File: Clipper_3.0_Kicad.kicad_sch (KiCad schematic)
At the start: 25 parts, among them J1 Conn_01x08_Pin, J10 Conn_01x19_Socket, J11 Screw_Terminal_01x02, J12 Conn_01x01_Socket, J13 Conn_01x01_Socket, J14 Conn_01x01_Socket, J15 Conn_01x01_Socket, J16 Conn_01x01_Pin, J17 Conn_01x01_Pin, J18 Conn_01x01_Pin, J19 Conn_01x01_Pin, J2 Conn_01x08_Pin, J3 Conn_01x08_Pin, J4 Conn_01x08_Socket, J5 Conn_01x08_Socket, J6 Conn_01x08_Socket, J7 Conn_01x19_Pin, J8 Conn_01x19_Pin, J9 Conn_01x19_Socket, M1 Motor_Derecho, M2 Motor_Îzquierdo, U1 ESP32-DevKitC, U2 TB6612FNG_MODULE, U3 GY-521 MODULE, U4 DC/DC MINI-360

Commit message: Actualizacion de avance en SCH
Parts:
- removed U1: ESP32-DevKitC, Espressif:ESP32-DevKitC, symbol PCM_Espressif:ESP32-DevKitC
- added C1: C_Polarized_Small, Capacitor_THT:CP_Radial_D8.0mm_P3.50mm, symbol Device:C_Polarized_Small
- added C2, C3, C4, C5, C6: C_Small, symbol Device:C_Small
- added J20: Screw_Terminal_01x02, TerminalBlock:TerminalBlock_Xinya_XY308-2.54-2P_1x02_P2.54mm_Horizontal, symbol Connector:Screw_Terminal_01x02
- added J21: Screw_Terminal_01x16, TerminalBlock:TerminalBlock_Xinya_XY308-2.54-16P_1x16_P2.54mm_Horizontal, symbol Connector:Screw_Terminal_01x16
- added U1: ESP32-DevKitC, Espressif:ESP32-DevKitC, symbol Personal:ESP32-DevKitC
- added U5: AMS1117-3.3, Package_TO_SOT_SMD:SOT-223-3_TabPin2, symbol Regulator_Linear:AMS1117-3.3
- added U6: CD74HC4067SM, Package_SO:SSOP-24_5.3x8.2mm_P0.65mm, symbol 74xx:CD74HC4067SM
- added U7, U8: QTR8-A, symbol Personal:QTR8-A
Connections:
- net I2C-CLK is gone; now on an unnamed net: U3.3 (SCL)
- net I2C-DATA is gone; now on an unnamed net: U3.4 (SDA)
- net VCC is gone; now on net VCC3.3V: J5.2 (Pin_2)
- net VM is gone; now on net VCC12V: J5.1 (Pin_1)
- net AIN1: now also J4.14 (Pin_3), J9.12 (Pin_12); no longer U2.14 (AIN1)
- net AIN2: now also J4.15 (Pin_2), J9.13 (Pin_13); no longer U2.15 (AIN2)
- net AO1: now also J20.1 (Pin_1); no longer M1.1 (+)
- net AO2: now also J20.2 (Pin_2); no longer M1.2 (-)
- net BIN1: now also J4.12 (Pin_5), J9.10 (Pin_10); no longer U2.12 (BIN1)
- net BIN2: now also J4.11 (Pin_6), J9.9 (Pin_9); no longer U2.11 (BIN2)
- net BO1: now also J11.2 (Pin_2); no longer M2.1 (+)
- net BO2: now also J11.1 (Pin_1); no longer M2.2 (-)
- net GND: now also J10.1 (Pin_1), J10.7 (Pin_7), J13.1 (Pin_1), J15.1 (Pin_1), J4.9 (Pin_8), J6.2 (Pin_2), J9.14 (Pin_14), C1.2, C2.2, C3.2, C4.2, C5.2, C6.2, J21.1 (Pin_1), J21.16 (Pin_16), J21.8 (Pin_8), U5.1 (GND), U6.12 (GND), U6.15 (~{E}), U7.1 (GND), U8.1 (GND)
- net PWMA: now also J4.16 (Pin_1), J9.15 (Pin_15); no longer U2.16 (PWMA)
- net PWMB: now also J4.10 (Pin_7), J9.8 (Pin_8); no longer U2.10 (PWMB)
- net STBY: now also J4.13 (Pin_4), J9.11 (Pin_11); no longer U2.13 (STBY)
- net at J3.1 (Pin_1): now also U3.1 (VCC)
- net at J3.2 (Pin_2): now also U3.2 (GND)
- net at J3.5 (Pin_5): now also U3.5 (XDA)
- net at J3.6 (Pin_6): now also U3.6 (XCL)
- net at J3.7 (Pin_7): now also U3.7 (AD0)
- net at J2.3 (Pin_3), J2.8 (Pin_8), U2.3,8,9 (GND): now also J1.9 (Pin_8)
- net at J7.1 (Pin_1): now also U1.38 (GND)
- net at J7.10 (Pin_10): now also U1.29 (GPIO5)
- net at J7.11 (Pin_11): now also U1.28 (GPIO17)
- net at J7.12 (Pin_12): now also U1.27 (GPIO16)
- net at J7.13 (Pin_13): now also U1.26 (ADC2_CH0/GPIO4)
- net at J7.14 (Pin_14): now also U1.25 (GPIO0/BOOT/ADC2_CH1)
- net at J7.15 (Pin_15): now also U1.24 (ADC2_CH2/GPIO2)
- net at J7.16 (Pin_16): now also U1.23 (MTDO/GPIO15/ADC2_CH3)
- net at J7.17 (Pin_17): now also U1.22 (SD_DATA1/GPIO8)
- net at J7.18 (Pin_18): now also U1.21 (SD_DATA0/GPIO7)
- net at J7.19 (Pin_19): now also U1.20 (SD_CLK/GPIO6)
- net at J7.2 (Pin_2): now also U1.37 (GPIO23)
- net at J7.3 (Pin_3): now also U1.36 (GPIO22)
- net at J7.4 (Pin_4): now also U1.35 (U0TXD/GPIO1)
- net at J7.5 (Pin_5): now also U1.34 (U0RXD/GPIO3)
- net at J7.6 (Pin_6): now also U1.33 (GPIO21)
- net at J7.7 (Pin_7): now also U1.32 (GND)
- net at J7.8 (Pin_8): now also U1.31 (GPIO19)
- net at J7.9 (Pin_9): now also U1.30 (GPIO18)
- net S1: now reaches J10.11 (Pin_11)
- net S1: now also J21.11 (Pin_11), U6.11 (S1)
- net S0: now reaches J10.12 (Pin_12)
- net S0: now also J21.10 (Pin_10), U6.10 (S0)
- net SIG: now reaches J10.13 (Pin_13)
- net SIG: now also J21.9 (Pin_9), U6.1 (COM)
- net at J10.17 (Pin_17): now also J21.7 (Pin_7)
- net LED: now reaches J10.18 (Pin_18)
- net LED: now also J21.6 (Pin_6)
- net BTN: now reaches J10.19 (Pin_19)
- net BTN: now also J21.5 (Pin_5)
- net ENCI: now reaches J10.2 (Pin_2)
- net ENCI: now also J21.14 (Pin_14)
- net at J10.3 (Pin_3): now also J6.3 (Pin_3)
- net at J10.6 (Pin_6): now also J6.4 (Pin_4)
- net S3: now reaches J10.8 (Pin_8)
- net S3: now also J21.13 (Pin_13), U6.13 (S3)
- net S2: now reaches J10.9 (Pin_9)
- net S2: now also J21.12 (Pin_12), U6.14 (S2)
- net VCC3.3V: now reaches J6.1 (Pin_1)
- net VCC3.3V: now also C5.1, C6.1, J21.15 (Pin_15), J21.3 (Pin_3), U5.2 (VO), U6.24 (VCC), U7.11 (VCC), U7.2 (IR), U8.11 (VCC), U8.2 (IR)
- net VCC5V: now reaches J9.19 (Pin_19)
- net VCC5V: now also J14.1 (Pin_1), C3.1, C4.1, U5.3 (VI)
- net ENCD: now reaches J9.7 (Pin_7)
- net ENCD: now also J21.4 (Pin_4)
- net VCC12V: now reaches J12.1 (Pin_1)
- net VCC12V: now also C1.1, C2.1, J21.2 (Pin_2)
- net at J8.1 (Pin_1): now also U1.1 (3V3)
- net at J8.10 (Pin_10): now also U1.10 (DAC_2/ADC2_CH9/GPIO26)
- net at J8.11 (Pin_11): now also U1.11 (ADC2_CH7/GPIO27)
- net at J8.12 (Pin_12): now also U1.12 (MTMS/GPIO14/ADC2_CH6)
- net at J8.13 (Pin_13): now also U1.13 (MTDI/GPIO12/ADC2_CH5)
- net at J8.14 (Pin_14): now also U1.14 (GND)
- net at J8.15 (Pin_15): now also U1.15 (MTCK/GPIO13/ADC2_CH4)
- net at J8.16 (Pin_16): now also U1.16 (SD_DATA2/GPIO9)
- net at J8.17 (Pin_17): now also U1.17 (SD_DATA3/GPIO10)
- net at J8.18 (Pin_18): now also U1.18 (CMD)
- net at J8.19 (Pin_19): now also U1.19 (5V)
- net at J8.2 (Pin_2): now also U1.2 (CHIP_PU)
- net at J8.3 (Pin_3): now also U1.3 (SENSOR_VP/GPIO36/ADC1_CH0)
- net at J8.4 (Pin_4): now also U1.4 (SENSOR_VN/GPIO39/ADC1_CH3)
- net at J8.5 (Pin_5): now also U1.5 (VDET_1/GPIO34/ADC1_CH6)
- net at J8.6 (Pin_6): now also U1.6 (VDET_2/GPIO35/ADC1_CH7)
- net at J8.7 (Pin_7): now also U1.7 (32K_XP/GPIO32/ADC1_CH4)
- net at J8.8 (Pin_8): now also U1.8 (32K_XN/GPIO33/ADC1_CH5)
- net at J8.9 (Pin_9): now also U1.9 (DAC_1/ADC2_CH8/GPIO25)
- new net: J1.10 (Pin_7), U2.10 (PWMB)
- new net: J1.11 (Pin_6), U2.11 (BIN2)
- new net: J1.12 (Pin_5), U2.12 (BIN1)
- new net: J1.13 (Pin_4), U2.13 (STBY)
- new net: J1.14 (Pin_3), U2.14 (AIN1)
- new net: J1.15 (Pin_2), U2.15 (AIN2)
- new net: J1.16 (Pin_1), U2.16 (PWMA)
- new net CH1_1: U6.9 (I0)
- new net CH1_2: U6.8 (I1)
- new net CH1_3: U6.7 (I2)
- new net CH1_4: U6.6 (I3)
- new net CH1_5: U6.5 (I4)
- new net CH1_6: U6.4 (I5)
- new net CH1_7: U6.3 (I6)
- new net CH1_8: U6.2 (I7)
- new net CH2_1: U6.23 (I8)
- new net CH2_2: U6.22 (I9)
- new net CH2_3: U6.21 (I10)
- new net CH2_4: U6.20 (I11)
- new net CH2_5: U6.19 (I12)
- new net CH2_6: U6.18 (I13)
- new net CH2_7: U6.17 (I14)
- new net CH2_8: U6.16 (I15)
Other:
- moved on the sheet: J10, J11, J12, J13, J14, J15, J16, J17, J18, J19, J2, J3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

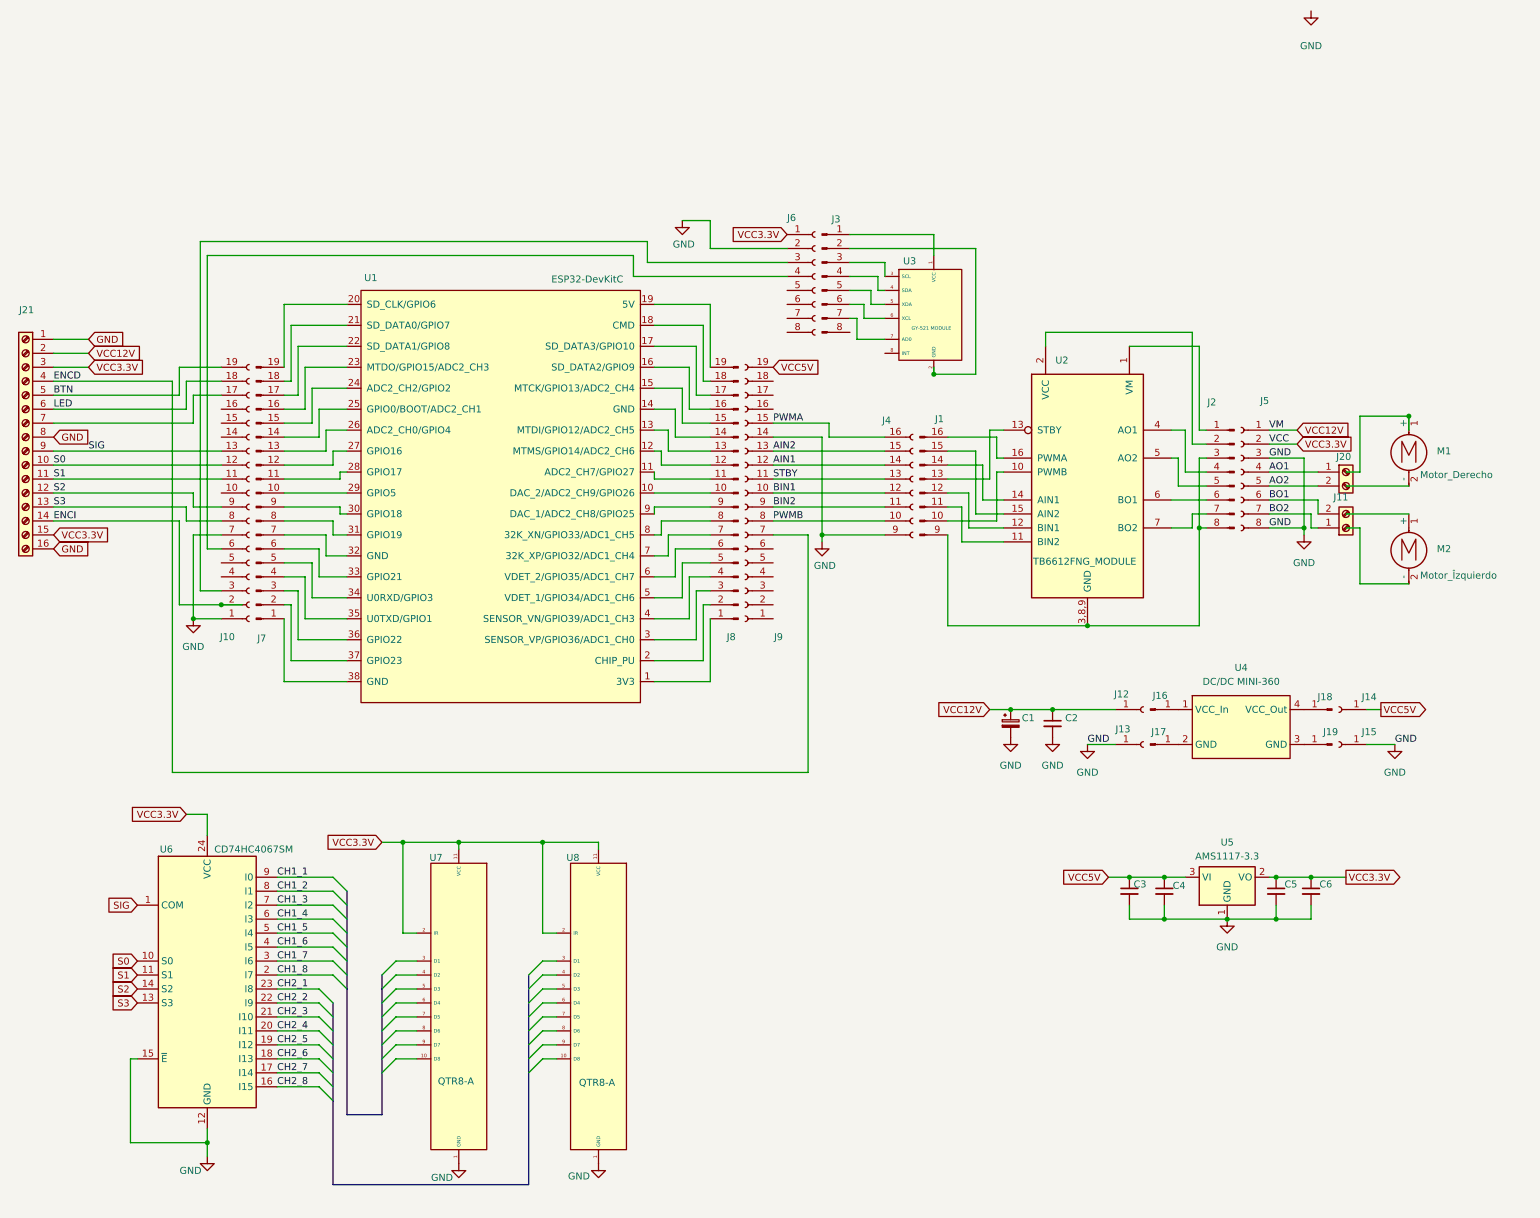
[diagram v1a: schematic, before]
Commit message: Terminacion del equematico y redistribucion de pines del ESP32 para evitar conflicto con wifi
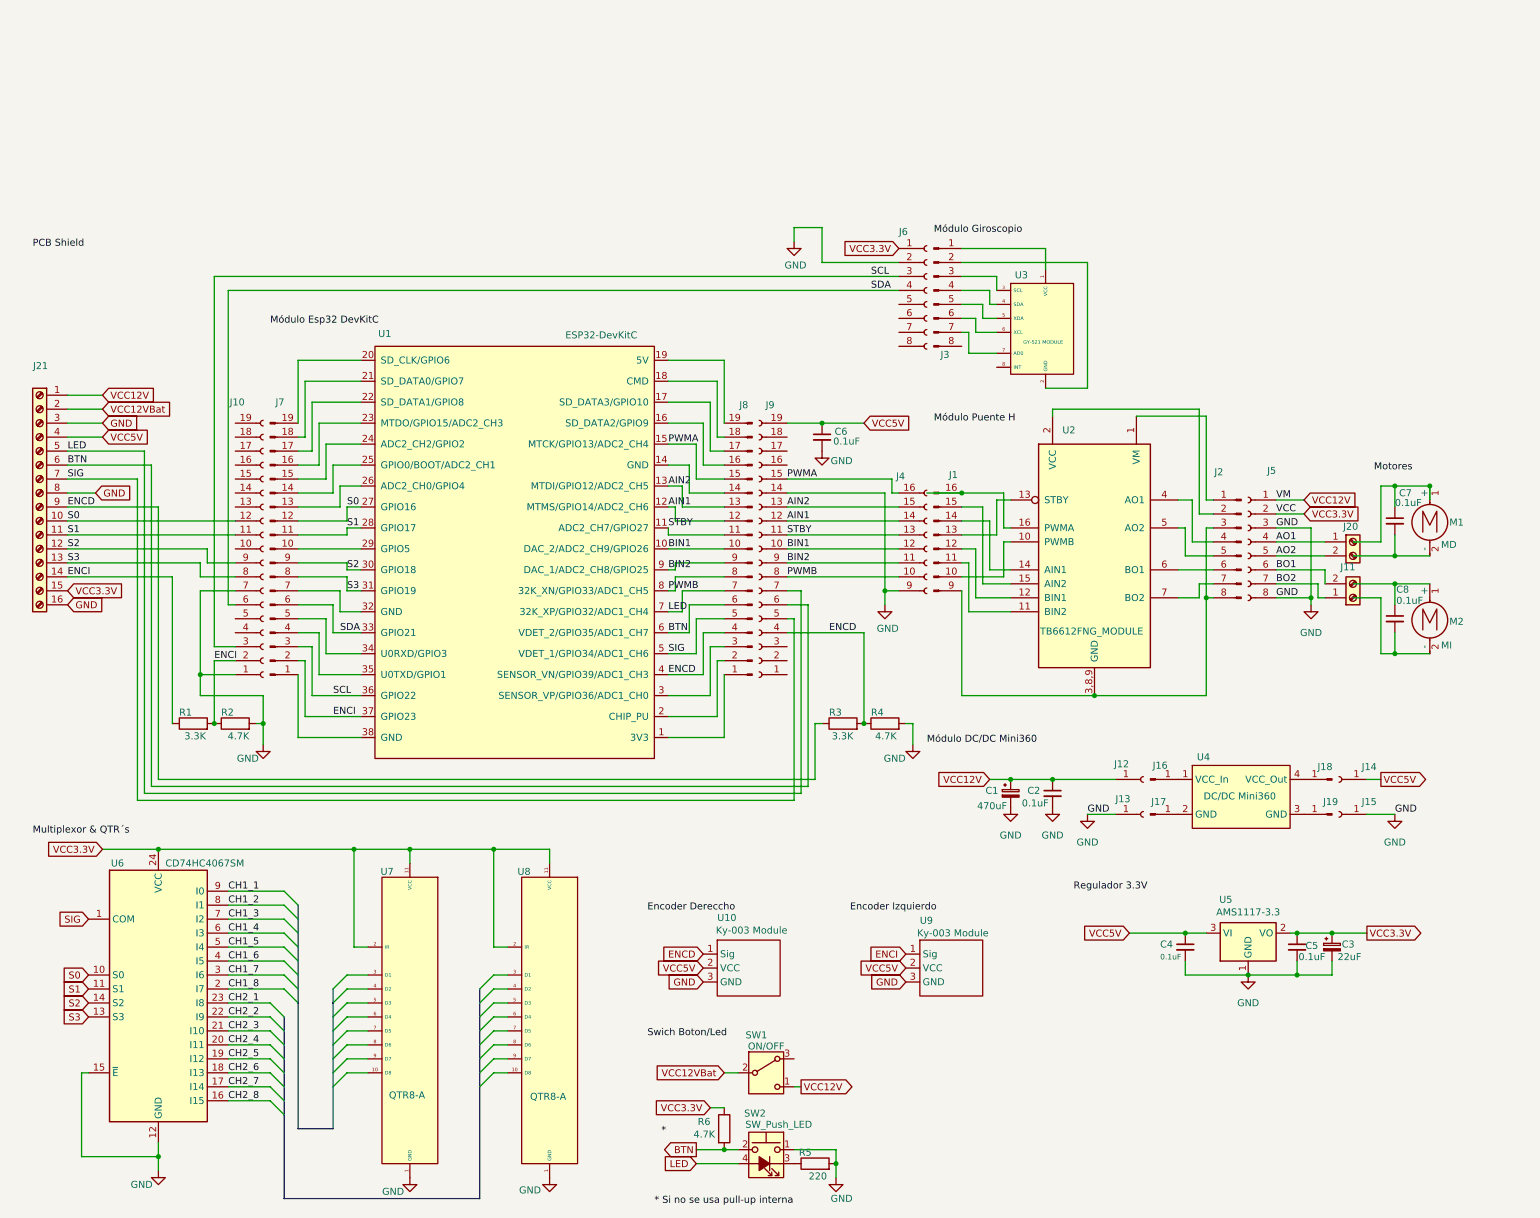
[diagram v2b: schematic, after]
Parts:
- removed C3: C_Small, symbol Device:C_Small
- added C3: 22uF, Capacitor_THT:CP_Radial_D5.0mm_P2.50mm, symbol Device:C_Polarized_Small
- added C7, C8: 0.1uF, symbol Device:C_Small
- added R1, R3: 3.3K, Resistor_SMD:R_1206_3216Metric_Pad1.30x1.75mm_HandSolder, symbol Device:R
- added R2, R4: 4.7K, Resistor_SMD:R_1206_3216Metric_Pad1.30x1.75mm_HandSolder, symbol Device:R
- added R5: 220, symbol Device:R
- added R6: 4.7K, symbol Device:R
- added SW1: ON/OFF, Button_Switch_SMD:Nidec_Copal_CAS-120A, symbol Switch:SW_Nidec_CAS-120A1
- added SW2: SW_Push_LED, symbol Switch:SW_Push_LED
- added U10, U9: Ky-003 Module, symbol Personal:Ky-003 Module
- C1: value C_Polarized_Small -> 470uF
- C2, C4, C5, C6: value C_Small -> 0.1uF; footprint (none) -> Capacitor_SMD:C_0805_2012Metric_Pad1.18x1.45mm_HandSolder
- M1: value Motor_Derecho -> MD
- M2: value Motor_Îzquierdo -> MI
- U4: value DC/DC MINI-360 -> DC/DC Mini360
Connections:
- net AIN1: now also J8.12 (Pin_12), U1.12 (MTMS/GPIO14/ADC2_CH6)
- net AIN2: now also J8.13 (Pin_13), U1.13 (MTDI/GPIO12/ADC2_CH5)
- net BIN1: now also J8.10 (Pin_10), U1.10 (DAC_2/ADC2_CH9/GPIO26)
- net BIN2: now also J8.9 (Pin_9), U1.9 (DAC_1/ADC2_CH8/GPIO25)
- net BTN: now also J21.6 (Pin_6), J8.6 (Pin_6), J9.6 (Pin_6), U1.6 (VDET_2/GPIO35/ADC1_CH7), R6.2, SW2.2; no longer J10.19 (Pin_19), J21.5 (Pin_5)
- net ENCD: now also J21.9 (Pin_9), J8.4 (Pin_4), J9.4 (Pin_4), U1.4 (SENSOR_VN/GPIO39/ADC1_CH3), R3.1, R3.2, R4.1, U10.1 (Sig); no longer J21.4 (Pin_4), J9.7 (Pin_7)
- net ENCI: now also J7.2 (Pin_2), U1.37 (GPIO23), R1.1, R1.2, R2.1, U9.1 (Sig)
- net GND: now also J21.3 (Pin_3), C3.2, R2.2, R4.2, R5.2, SW2.1, U10.3 (GND), U9.3 (GND); no longer J21.1 (Pin_1)
- net LED: now also J21.5 (Pin_5), J8.7 (Pin_7), J9.7 (Pin_7), U1.7 (32K_XP/GPIO32/ADC1_CH4), SW2.4 (A); no longer J10.18 (Pin_18), J21.6 (Pin_6)
- net PWMA: now also J8.15 (Pin_15), U1.15 (MTCK/GPIO13/ADC2_CH4)
- net PWMB: now also J8.8 (Pin_8), U1.8 (32K_XN/GPIO33/ADC1_CH5)
- net S0: now also J7.12 (Pin_12), U1.27 (GPIO16)
- net S1: now also J7.11 (Pin_11), U1.28 (GPIO17)
- net S2: now also J7.9 (Pin_9), U1.30 (GPIO18)
- net S3: now also J7.8 (Pin_8), U1.31 (GPIO19)
- net SIG: now also J21.7 (Pin_7), J8.5 (Pin_5), J9.5 (Pin_5), U1.5 (VDET_1/GPIO34/ADC1_CH6); no longer J10.13 (Pin_13), J21.9 (Pin_9)
- net STBY: now also J8.11 (Pin_11), U1.11 (ADC2_CH7/GPIO27)
- net VCC12V: now also J21.1 (Pin_1), SW1.1 (C); no longer J21.2 (Pin_2)
- net VCC3.3V: now also C3.1, R6.1; no longer C6.1, J21.3 (Pin_3)
- net VCC5V: now also C6.1, J21.4 (Pin_4), U10.2 (VCC), U9.2 (VCC)
- net at J10.17 (Pin_17): no longer J21.7 (Pin_7)
- net at M1.1 (+): now also C7.1
- net at M1.2 (-): now also C7.2
- net SCL: now reaches J7.3 (Pin_3), U1.36 (GPIO22)
- net SCL: now also J10.3 (Pin_3), J6.3 (Pin_3)
- net SDA: now reaches J7.6 (Pin_6), U1.33 (GPIO21)
- net SDA: now also J10.6 (Pin_6), J6.4 (Pin_4)
- net at M2.1 (+): now also C8.1
- net at M2.2 (-): now also C8.2
- new net: R5.1, SW2.3 (K)
- new net VCC12VBat: J21.2 (Pin_2), SW1.2 (B)
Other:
- company: (none) -> Ctrl+Alt+Robot
- title: (none) -> Clipper 
- moved on the sheet: C1, C2, C4, C5, J1, J10, J11, J12, J13, J14, J15, J16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
